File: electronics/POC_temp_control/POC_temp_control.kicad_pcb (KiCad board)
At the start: 2 copper layers, 2 parts

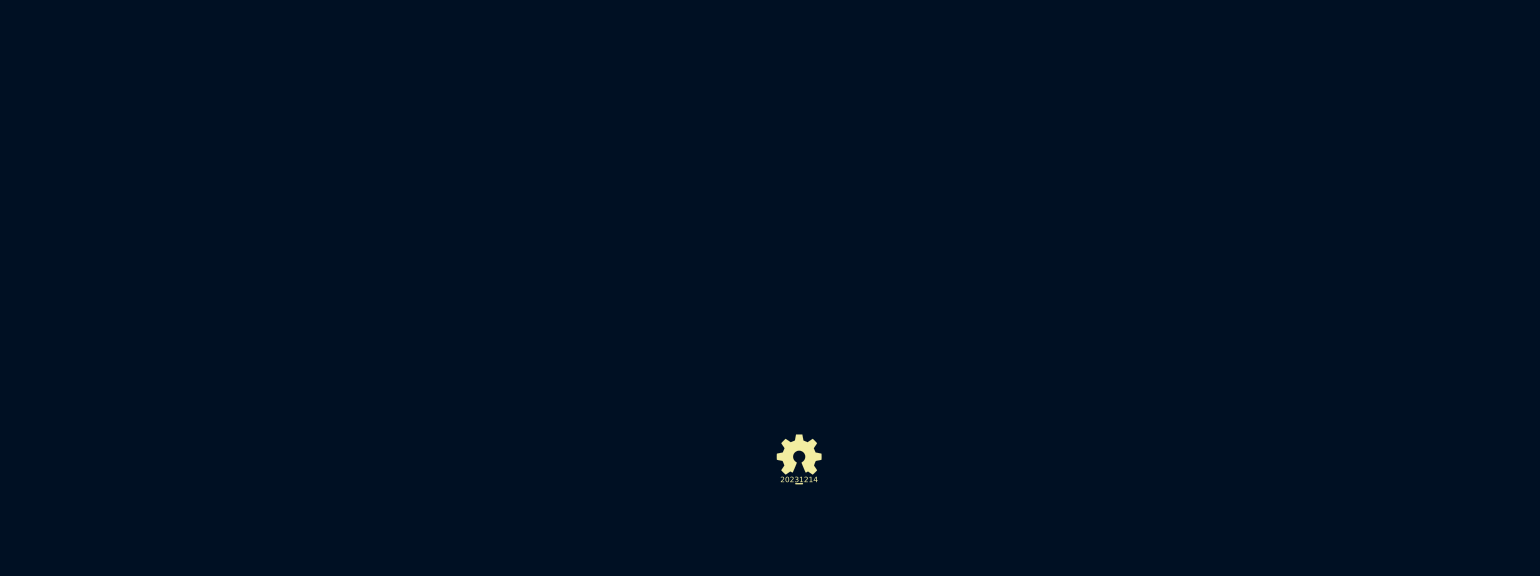
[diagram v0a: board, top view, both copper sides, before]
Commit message: added digital supplies and P&R
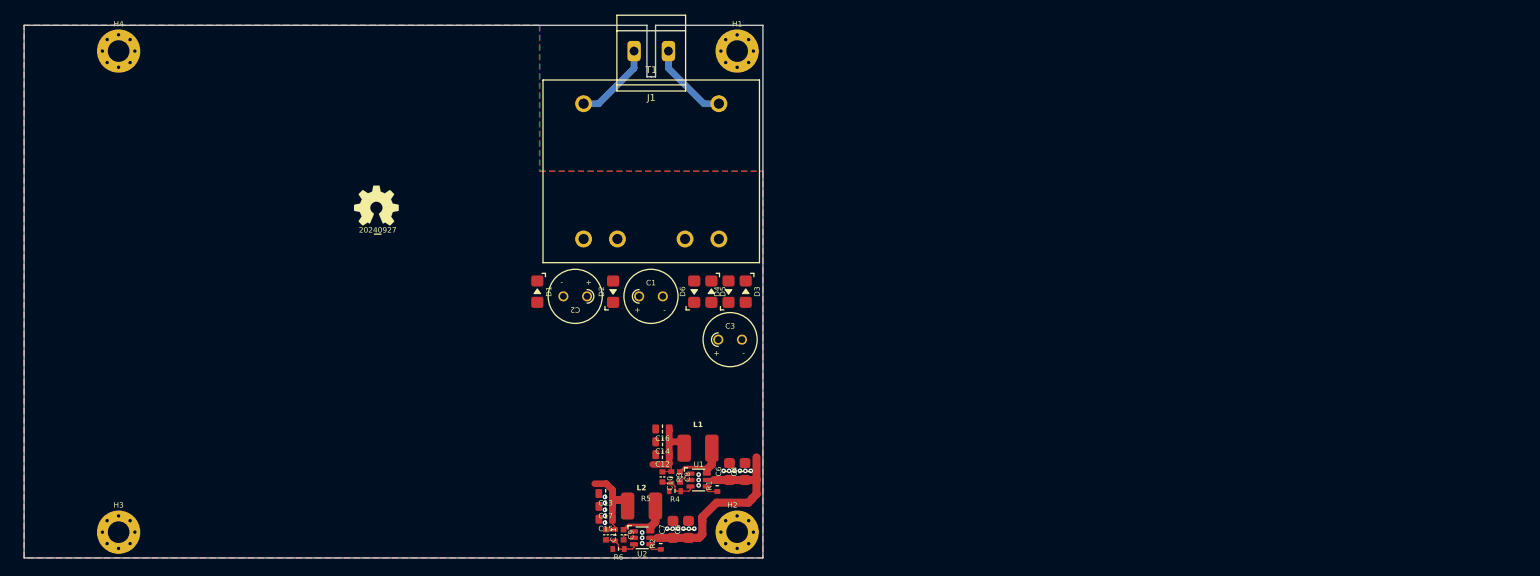
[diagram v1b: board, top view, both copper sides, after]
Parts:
- removed the N1 at (138.7, 91.3)
- added C1: 470uF 35V, SquantorCapacitor:C-035-080-elco, F.Cu at (116.8, 64.2)
- added C10: 47p, SquantorCapacitor:C_0603, F.Cu at (118.5, 90.9)
- added C11: 47p, SquantorCapacitor:C_0603, F.Cu at (110.2, 99.5)
- added C12: 10u, SquantorCapacitor:C_0805, F.Cu at (118.5, 87.6)
- added C13: 10u, SquantorCapacitor:C_0805, F.Cu at (110.1, 93.3)
- added C14: 10u, SquantorCapacitor:C_0805, F.Cu at (118.5, 85.7)
- added C15: 10u, SquantorCapacitor:C_0805, F.Cu at (110.1, 97.2)
- added C16: 10u, SquantorCapacitor:C_0805, F.Cu at (118.5, 83.8)
- added C17: 10u, SquantorCapacitor:C_0805, F.Cu at (110.1, 95.2)
- added C2: 470uF 35V, SquantorCapacitor:C-035-080-elco, F.Cu at (105.6, 64.2)
- added C3: 470uF 35V, SquantorCapacitor:C-035-080-elco, F.Cu at (128.5, 70.6)
- added C4: 10u, SquantorCapacitor:C_1206_0805, F.Cu at (130.7, 90.1)
- added C5: 10u, SquantorCapacitor:C_1206_0805, F.Cu at (122.3, 98.7)
- added C6: 10u, SquantorCapacitor:C_1206_0805, F.Cu at (128.4, 90.1)
- added C7: 10u, SquantorCapacitor:C_1206_0805, F.Cu at (120.0, 98.7)
- added C8: 100n, SquantorCapacitor:C_0603, F.Cu at (121.1, 90.9)
- added C9: 100n, SquantorCapacitor:C_0603, F.Cu at (112.8, 99.5)
- added D1: D, SquantorDiodes:SOD-123F-hand, F.Cu at (100.0, 63.5)
- added D2: D, SquantorDiodes:SOD-123F-hand, F.Cu at (111.2, 63.5)
- added D3: D, SquantorDiodes:SOD-123F-hand, F.Cu at (130.8, 63.5)
- added D4: D, SquantorDiodes:SOD-123F-hand, F.Cu at (128.3, 63.5)
- added D5: D, SquantorDiodes:SOD-123F-hand, F.Cu at (125.7, 63.5)
- added D6: D, SquantorDiodes:SOD-123F-hand, F.Cu at (123.2, 63.5)
- added H1: MountingHole, SquantorPcbOutline:MountingHole_3.2mm_M3_Pad_Via, F.Cu at (129.5, 27.9)
- added H2: MountingHole, SquantorPcbOutline:MountingHole_3.2mm_M3_Pad_Via, F.Cu at (129.5, 99.1)
- added H3: MountingHole, SquantorPcbOutline:MountingHole_3.2mm_M3_Pad_Via, F.Cu at (38.1, 99.1)
- added H4: MountingHole, SquantorPcbOutline:MountingHole_3.2mm_M3_Pad_Via, F.Cu at (38.1, 27.9)
- added J1: Conn_01x02, SquantorPhoenixContact:MKDS_2conn_508pitch_1711725, F.Cu at (116.8, 27.9)
- added L1: TBD, SquantorInductor:L_VLS50XXEX_TDK_hand, F.Cu at (123.8, 86.7)
- added L2: TBD, SquantorInductor:L_VLS50XXEX_TDK_hand, F.Cu at (115.4, 95.2)
- added N2: 20240927, SquantorLabels:Label_Generic, F.Cu at (76.4, 54.4)
- added R1: 100k, SquantorResistor:R_0603_hand, F.Cu at (126.6, 92.2)
- added R2: 100k, SquantorResistor:R_0603_hand, F.Cu at (118.2, 100.8)
- added R3: 100K, SquantorResistor:R_0603_hand, F.Cu at (119.8, 91.0)
- added R4: 22K, SquantorResistor:R_0603_hand, F.Cu at (120.3, 93.0)
- added R5: 110K, SquantorResistor:R_0603_hand, F.Cu at (111.5, 99.5)
- added R6: 15K, SquantorResistor:R_0603_hand, F.Cu at (112.0, 101.5)
- added T1: 10P_1P_2S, SquantorTransformer:10pin_5pitch_32x27_1Pri_2Sec, F.Cu at (116.8, 45.7)
- added U1: SY8120, SquantorIC:SOT23-6-HAND, F.Cu at (123.8, 91.3)
- added U2: SY8120, SquantorIC:SOT23-6-HAND, F.Cu at (115.5, 99.9)
- moved N1 72.5 mm to (76.2, 50.8)
- renumbered N2 to N1
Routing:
- net /VD+: track 0.00 -> 32.2 mm
- net /+5VD: track 0.00 -> 13.1 mm
- net /+3.3VD: track 0.00 -> 12.5 mm
- net /LINE: track 0.00 -> 12.2 mm
- net /NEUT: track 0.00 -> 12.2 mm
- net Net-(U2-LX): track 0.00 -> 9.24 mm
- net Net-(U1-LX): track 0.00 -> 8.45 mm
- net /FB5V: track 0.00 -> 5.56 mm
- net /FB33: track 0.00 -> 5.56 mm
- net Net-(U2-BS): track 0.00 -> 2.39 mm
- net Net-(U2-EN): track 0.00 -> 2.18 mm
- net Net-(U1-EN): track 0.00 -> 2.18 mm
- net Net-(U1-BS): track 0.00 -> 2.08 mm
- net /GND: vias 0 -> 23
- added copper zone on B.Cu, net /GND
- added copper zone on F.Cu, net /GND
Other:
- board outline added: 109.2 x 78.7 mm

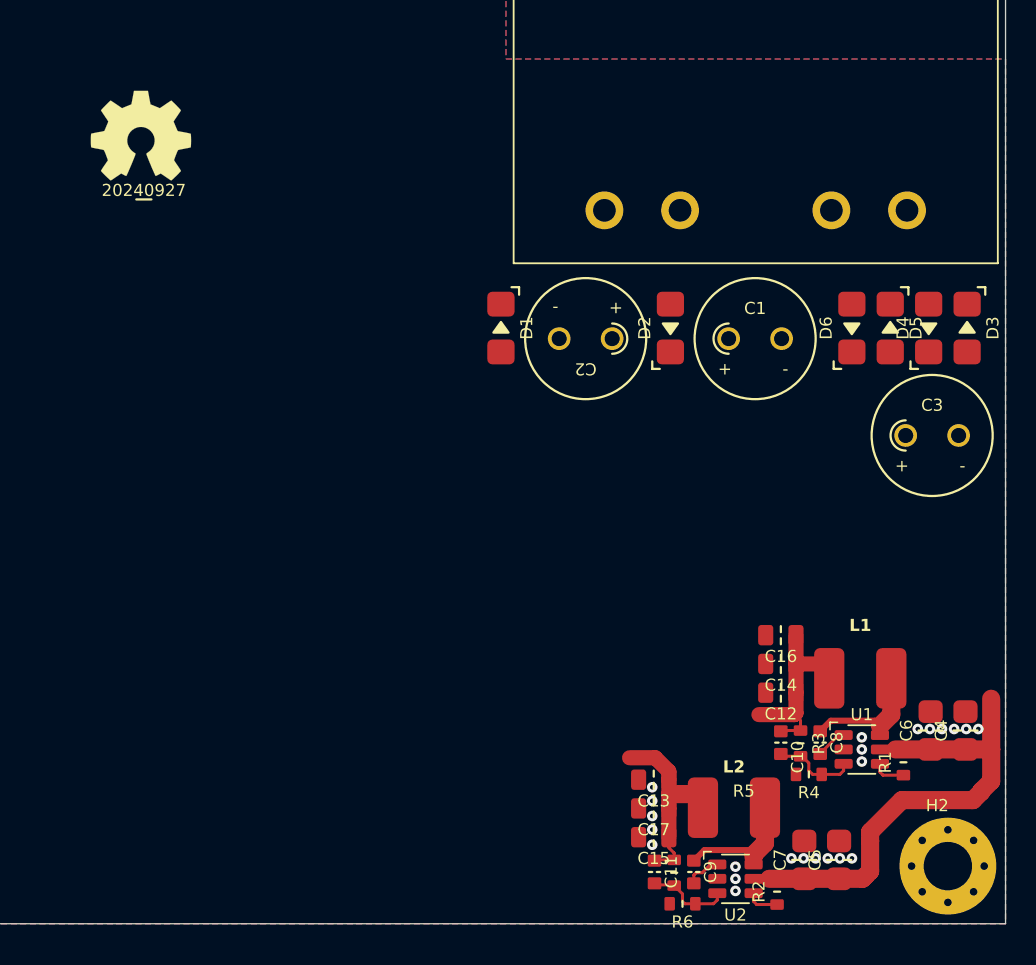
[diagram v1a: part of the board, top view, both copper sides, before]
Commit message: added analog powersupply
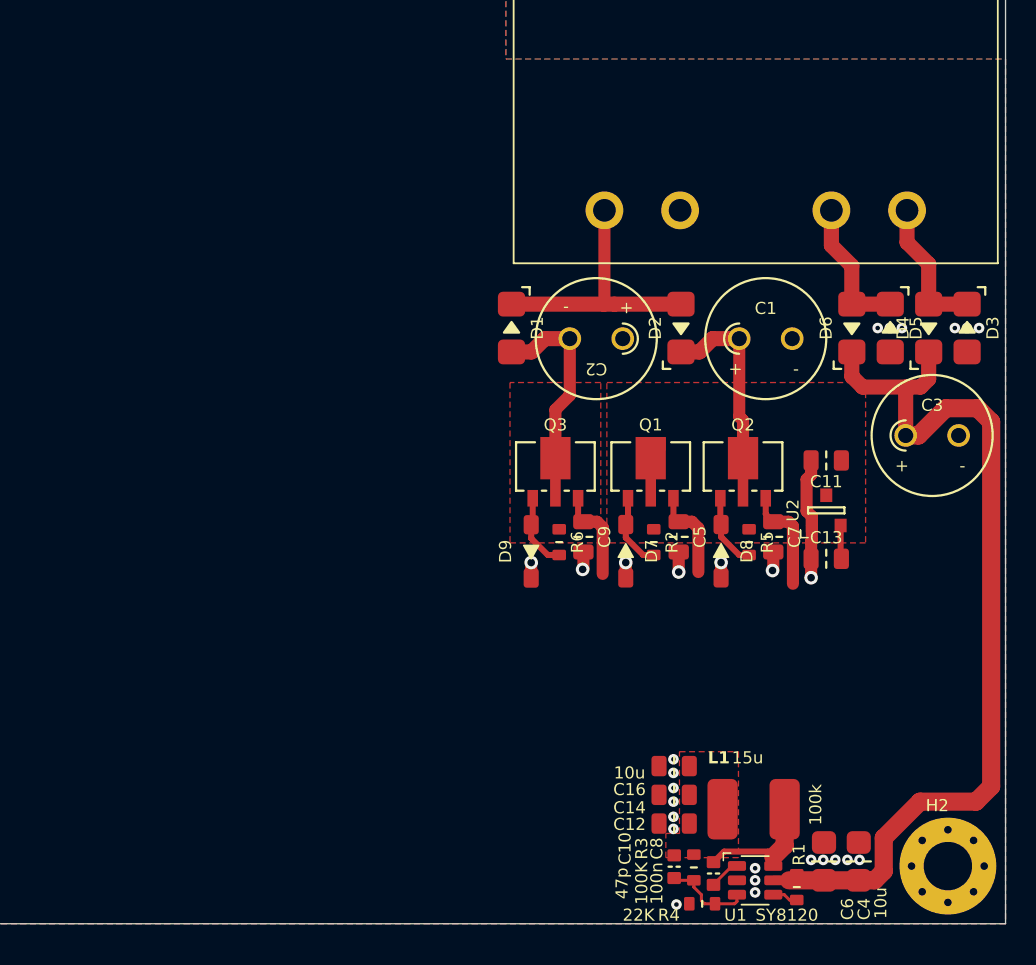
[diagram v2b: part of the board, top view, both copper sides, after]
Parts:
- removed C15, C17: 10u, SquantorCapacitor:C_0805
- removed L2: TBD, SquantorInductor:L_VLS50XXEX_TDK_hand
- added D7: 5.6V, SquantorDiodes:SOD-123-hand, F.Cu at (108.2, 78.2)
- added D8: 8.7V, SquantorDiodes:SOD-123-hand, F.Cu at (114.5, 78.2)
- added D9: 5.1V, SquantorDiodes:SOD-123-hand, F.Cu at (102.0, 78.3)
- added Q1: PXT8050, SquantorIC:SOT89-NXP, F.Cu at (109.9, 73.0)
- added Q2: PXT8050, SquantorIC:SOT89-NXP, F.Cu at (116.0, 73.0)
- added Q3: PXT8550, SquantorIC:SOT89-NXP, F.Cu at (103.6, 73.0)
- C11: value 47p -> 10u; footprint SquantorCapacitor:C_0603 -> SquantorCapacitor:C_0805
- C5, C7: footprint SquantorCapacitor:C_1206_0805 -> SquantorCapacitor:C_0805
- C9: value 100n -> 10u; footprint SquantorCapacitor:C_0603 -> SquantorCapacitor:C_0805
- L1: value TBD -> 15u
- N1, N2: moved to B.Cu
- R2: value 100k -> 2K7
- R5: value 110K -> 470
- R6: value 15K -> 2K7
- U2: value SY8120 -> MCP1702T-3302; footprint SquantorIC:SOT23-6-HAND -> SquantorIC:SOT23-3
- moved N1 41.0 mm to (116.8, 45.7), turned to 180 degrees
- moved N2 40.6 mm to (116.6, 49.3), turned to 180 degrees
- moved C11 29.5 mm to (121.5, 72.2), turned to 180 degrees
- moved R6 25.3 mm to (103.8, 77.7), turned to -90 degrees
- moved U2 25.1 mm to (121.5, 75.5), turned to 90 degrees
- moved R2 24.5 mm to (110.1, 77.7), turned to -90 degrees
- moved C5 23.8 mm to (111.8, 77.3), turned to -90 degrees
- moved C9 23.3 mm to (105.5, 77.3)
- moved R5 22.4 mm to (116.4, 77.7)
- moved C7 21.4 mm to (118.0, 77.3), turned to -90 degrees
- moved C13 18.5 mm to (121.5, 78.8), turned to 0 degrees
- moved C6 11.2 mm to (121.3, 98.8)
- moved C12 11.2 mm to (111.5, 96.2)
- moved C16 11.2 mm to (111.5, 92.5)
- moved U1 11.2 mm to (116.8, 100.0)
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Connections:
- C11 pad 1: /+3.3VD -> /VA+
- C11 pad 2: /FB33 -> /GND
- C13 pad 1: /+3.3VD -> /GND
- C13 pad 2: /GND -> /VA3.3V+
- C5 pad 1: /VD+ -> /VA4.9V+
- C7 pad 1: /VD+ -> /VA8V+
- C9 pad 1: Net-(U2-LX) -> /VA4.5V-
- C9 pad 2: Net-(U2-BS) -> /GND
- R2 pad 1: Net-(U2-EN) -> /VA+
- R2 pad 2: /VD+ -> Net-(D7-K)
- R5 pad 1: /+3.3VD -> /VA+
- R5 pad 2: /FB33 -> Net-(D8-K)
- R6 pad 1: /FB33 -> /VA-
- R6 pad 2: /GND -> Net-(D9-A)
- U2 pad 1: Net-(U2-BS) -> /GND
- U2 pad 2: /GND -> /VA3.3V+
- U2 pad 3: /FB33 -> /VA+
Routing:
- net /VD+: track 32.2 -> 61.1 mm
- net Net-(D1-K): track 0.00 -> 17.4 mm
- net /GND: track 0.00 -> 14.8 mm, vias 23 -> 28
- net /VA-: track 0.00 -> 12.5 mm
- net /+3.3VD: track 12.5 -> 0.00 mm
- net /VA+: track 0.00 -> 12.2 mm
- net /+5VD: track 13.1 -> 1.12 mm
- net Net-(D3-K): track 0.00 -> 9.33 mm
- net Net-(D5-K): track 0.00 -> 9.30 mm
- net Net-(U2-LX): track 9.24 -> 0.00 mm
- net /VA8V+: track 0.00 -> 6.98 mm
- net /VA4.5V-: track 0.00 -> 6.20 mm
- net /VA4.9V+: track 0.00 -> 6.07 mm
- net /FB33: track 5.56 -> 0.00 mm
- net Net-(D9-A): track 0.00 -> 5.00 mm
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- added copper zone on F.Cu, net /+5VD
- added copper zone on F.Cu, net /VA+
- added copper zone on F.Cu, net /VA-

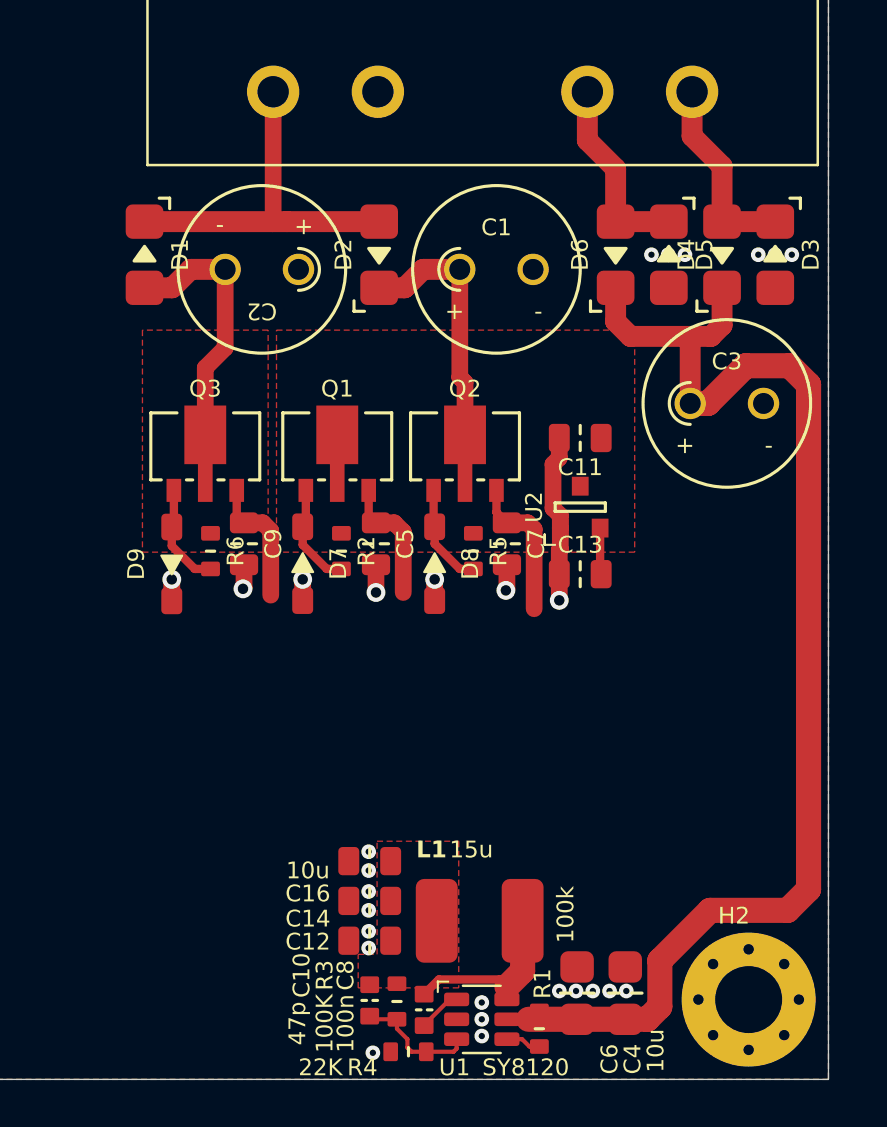
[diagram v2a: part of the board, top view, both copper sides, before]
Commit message: added analog supplies, started with nuclone addition
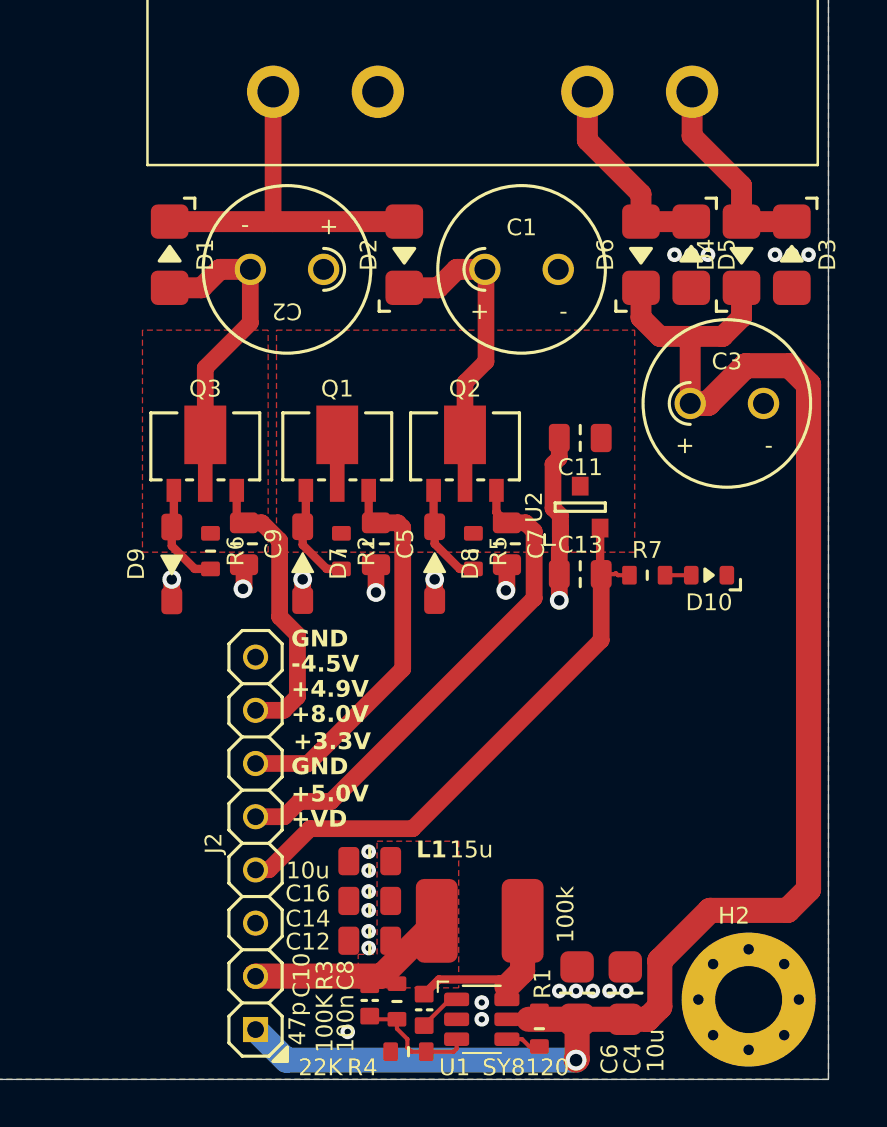
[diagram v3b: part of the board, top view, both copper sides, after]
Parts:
- added D10: GRN, SquantorDiodes:LED_0603_hand, F.Cu at (127.7, 78.8)
- added J2: Conn_01x07, SquantorConnectors:Header-0254-1X08-H008, F.Cu at (106.0, 91.6)
- added R7: 1k, SquantorResistor:R_0603_hand, F.Cu at (124.7, 78.8)
- moved D6 1.21 mm to (124.4, 63.5)
- moved C1 1.20 mm to (118.7, 64.2)
- moved C2 1.20 mm to (107.5, 64.2)
- moved D1 1.20 mm to (101.9, 63.5)
- moved D2 1.20 mm to (113.1, 63.5)
- moved D5 1.07 mm to (126.8, 63.5)
- moved D4 0.93 mm to (129.2, 63.5)
- moved D3 0.79 mm to (131.6, 63.5)
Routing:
- net /VA3.3V+: track 2.22 -> 27.8 mm
- net /VD+: track 61.1 -> 78.3 mm, vias 0 -> 1
- net /VA8V+: track 6.98 -> 24.0 mm
- net /VA4.9V+: track 6.07 -> 18.7 mm
- net /+5VD: track 1.12 -> 10.9 mm
- net /VA4.5V-: track 6.20 -> 13.8 mm
- net Net-(D10-A): track 0.00 -> 1.25 mm
- net /GND: vias 28 -> 27
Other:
- board text added: "+3.3V"
- board text added: "+4.9V"
- board text added: "+5.0V"
- board text added: "+8.0V"
- board text added: "+VD"
- board text added: "-4.5V"
- board text added: "GND"
